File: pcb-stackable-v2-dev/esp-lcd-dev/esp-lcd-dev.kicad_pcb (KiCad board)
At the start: 2 copper layers, 40 x 40 mm, 37 parts, among them J1 JST XH/PH, J2 Qwiic, J3 Qwiic, J4 STEMMA-Signal, J5 JST SH, J6 Pin headers, Q1 2N7002DW, U1 VEML7700

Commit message: Add SMD pin sockets for LCD module on esp-lcd-dev
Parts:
- added J7: Pin headers, Connector_PinSocket_2.54mm:PinSocket_1x04_P2.54mm_Vertical_SMD_Pin1Right, F.Cu at (91.1, 68.8)
- added J8: Pin headers, Connector_PinSocket_2.54mm:PinSocket_1x04_P2.54mm_Vertical_SMD_Pin1Left, F.Cu at (108.9, 68.8)
- moved G*** 16.6 mm to (92.2, 76.5)
- moved REF** 6.18 mm to (99.8, 73.0)
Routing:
- net LCD_CS: track 10.9 -> 40.3 mm, vias 1 -> 4
- net LCD_RESET: track 14.7 -> 37.5 mm, vias 1 -> 3
- net SPI_MOSI: track 8.37 -> 30.4 mm, vias 1 -> 3
- net LCD_DC: track 10.8 -> 26.5 mm, vias 1 -> 4
- net LCD_BACKLIGHT: track 12.7 -> 27.3 mm, vias 1 -> 2
- net +3V3: track 120.9 -> 130.5 mm, vias 7 -> 8
- net SPI_CLK: track 11.9 -> 21.4 mm, vias 1 -> 2
- net NEOPIXEL_2_DATA_5V: track 49.6 -> 54.7 mm
- net SCL: track 64.7 -> 61.7 mm
- net STATUS_LED: track 35.6 -> 36.5 mm
- net GND: vias 14 -> 18
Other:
- board text added: "ESP32-C3"
- board text added: "LCD Dev"
- board text removed: "ESP32-C3 LCD Dev"
- board text removed: "github.com/smkent/pcb"

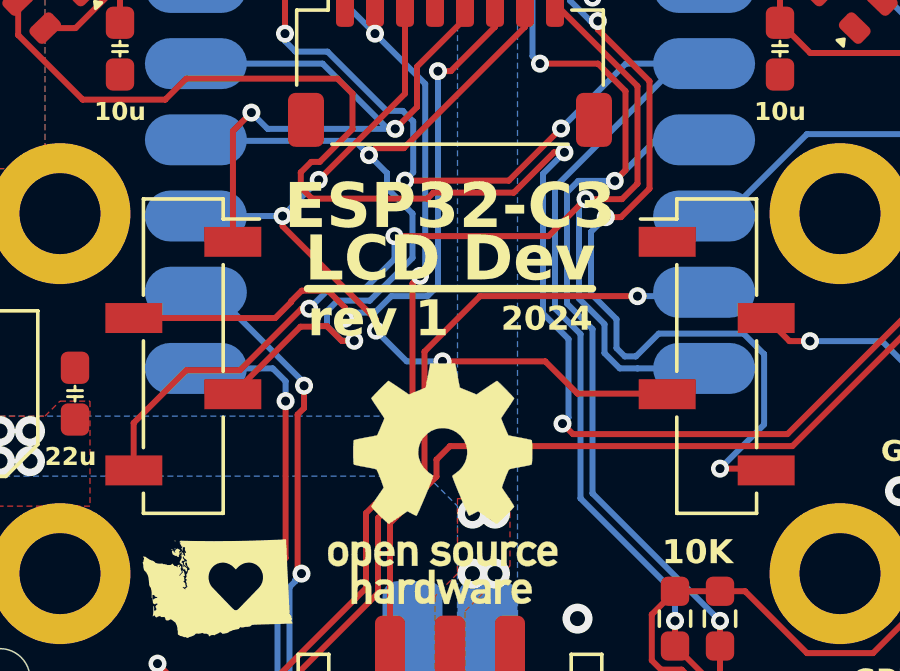
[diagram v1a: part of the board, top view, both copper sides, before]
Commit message: Label pin sockets on silkscreen on esp-lcd-dev
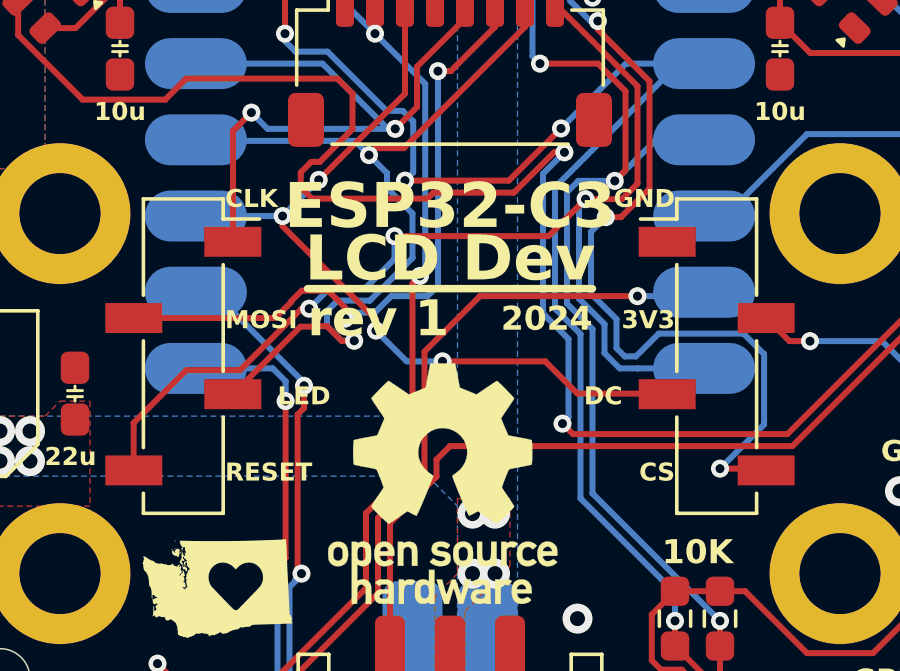
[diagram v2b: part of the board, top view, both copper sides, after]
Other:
- board text added: "MOSI"
- board text added: "RESET"
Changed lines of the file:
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@@
+		)
+	)
+	(gr_text "CLK"
+		(at 92.5 63.5 0)
+		(layer "F.SilkS")
+		(effects
+			(font
+				(size 0.6 0.6)
+				(thickness 0.12)
+				(bold yes)
+			)
+			(justify left)
 		)
 	)
@@
 	)
 	(gr_text "CS"
+		(at 107.5 72.62 0)
+		(layer "F.SilkS")
+		(effects
+			(font
+				(size 0.6 0.6)
+				(thickness 0.12)
+				(bold yes)
+			)
+			(justify right)
+		)
+	)
+	(gr_text "CS"
 		(at 99.5 56.25 -90)
 		(layer "F.SilkS")
@@
 	(gr_text "DC"
 		(at 98.5 56.25 -90)
+		(layer "F.SilkS")
+		(effects
+			(font
+				(size 0.6 0.6)
+				(thickness 0.12)
+				(bold yes)
+			)
+			(justify right)
+		)
+	)
+	(gr_text "GND"
+		(at 107.5 63.5 0)
 		(layer "F.SilkS")
 		(effects
@@
 		)
 	)
+	(gr_text "DC"
+		(at 105.75 70.08 0)
+		(layer "F.SilkS")
+		(effects
+			(font
+				(size 0.6 0.6)
+				(thickness 0.12)
+				(bold yes)
+			)
+			(justify right)
+		)
+	)
 	(gr_text "RES"
 		(at 103.5 56.25 -90)
@@
 		)
 	)
+	(gr_text "LED"
+		(at 94.25 70.08 0)
+		(layer "F.SilkS")
+		(effects
+			(font
+				(size 0.6 0.6)
+				(thickness 0.12)
+				(bold yes)
+			)
+			(justify left)
+		)
+	)
 	(gr_text "2xN"
 		(at 117.25 62.5 -90)
@@
 		)
 	)
+	(gr_text "RESET"
+		(at 92.5 72.62 0)
+		(layer "F.SilkS")
+		(effects
+			(font
+				(size 0.6 0.6)
+				(thickness 0.12)
+				(bold yes)
+			)
+			(justify left)
+		)
+	)
+	(gr_text "3V3"
+		(at 107.5 67.54 0)
+		(layer "F.SilkS")
+		(effects
+			(font
+				(size 0.6 0.6)
+				(thickness 0.12)
+				(bold yes)
+			)
+			(justify right)
+		)
+	)
 	(gr_text "G7"
 		(at 116.75 77 0)
@@
 		)
 	)
+	(gr_text "MOSI"
+		(at 92.5 67.54 0)
+		(layer "F.SilkS")
+		(effects
+			(font
+				(size 0.6 0.6)
+				(thickness 0.12)
+				(bold yes)
+			)
+			(justify left)
+		)
+	)
